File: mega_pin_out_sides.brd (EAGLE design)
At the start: 100 x 85 mm, 102 parts, among them T1 2N2222, T10 2N2222, T11 2N2222, T12 2N2222, T13 2N2222, T14 2N2222, T15 2N2222, T16 2N2222, T17 2N2222, T18 2N2222, T2 2N2222, T3 2N2222, T4 2N2222, T5 2N2222, T6 2N2222, T7 2N2222, T8 2N2222, T9 2N2222

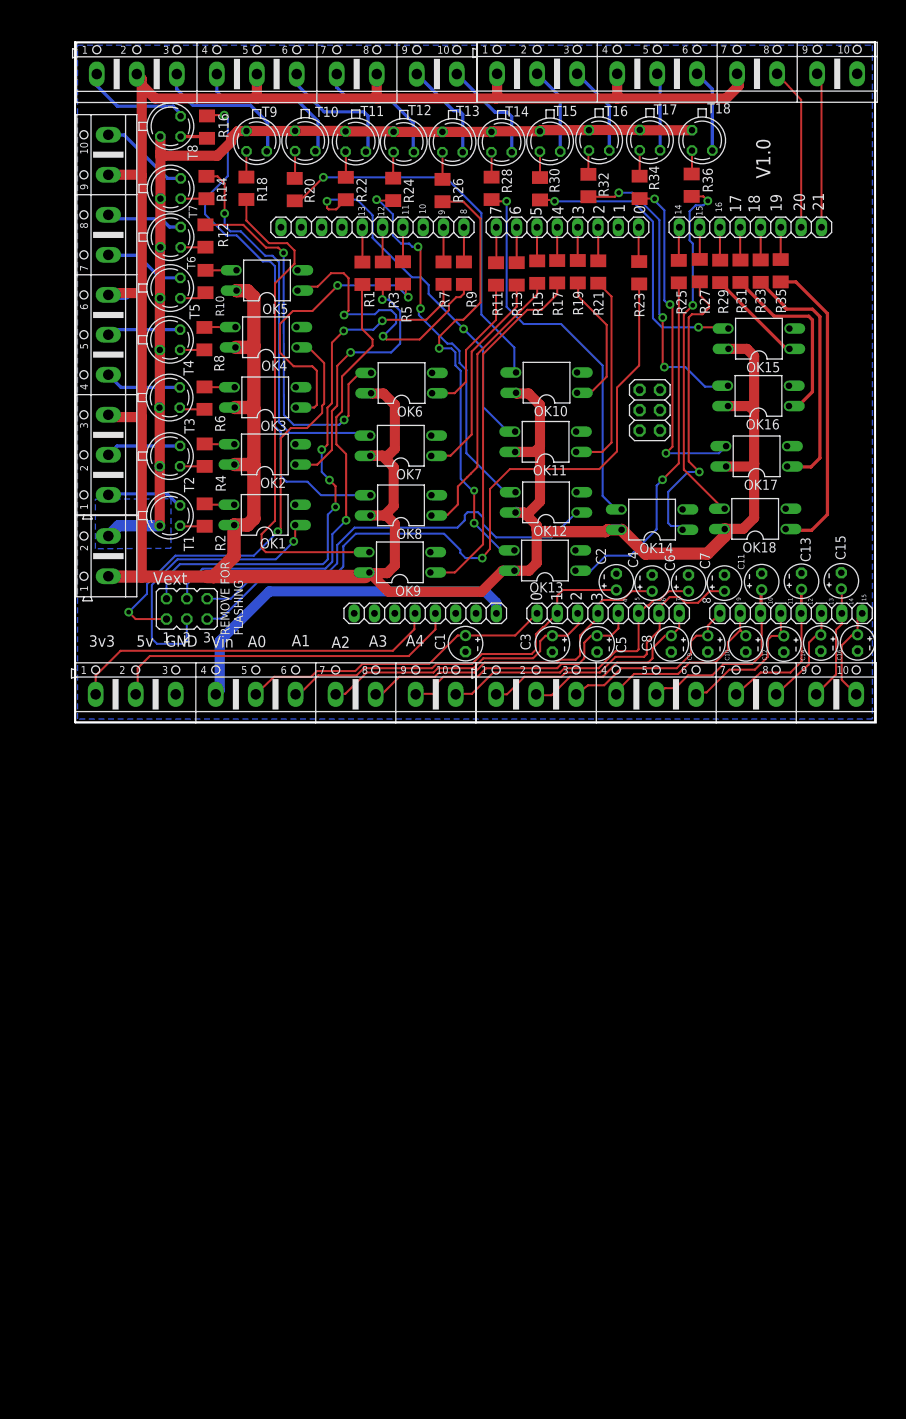
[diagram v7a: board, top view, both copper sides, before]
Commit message: [SIDES] Review of board and enhancements
- changed capacitors orientation. 
- Changed some pcb traces
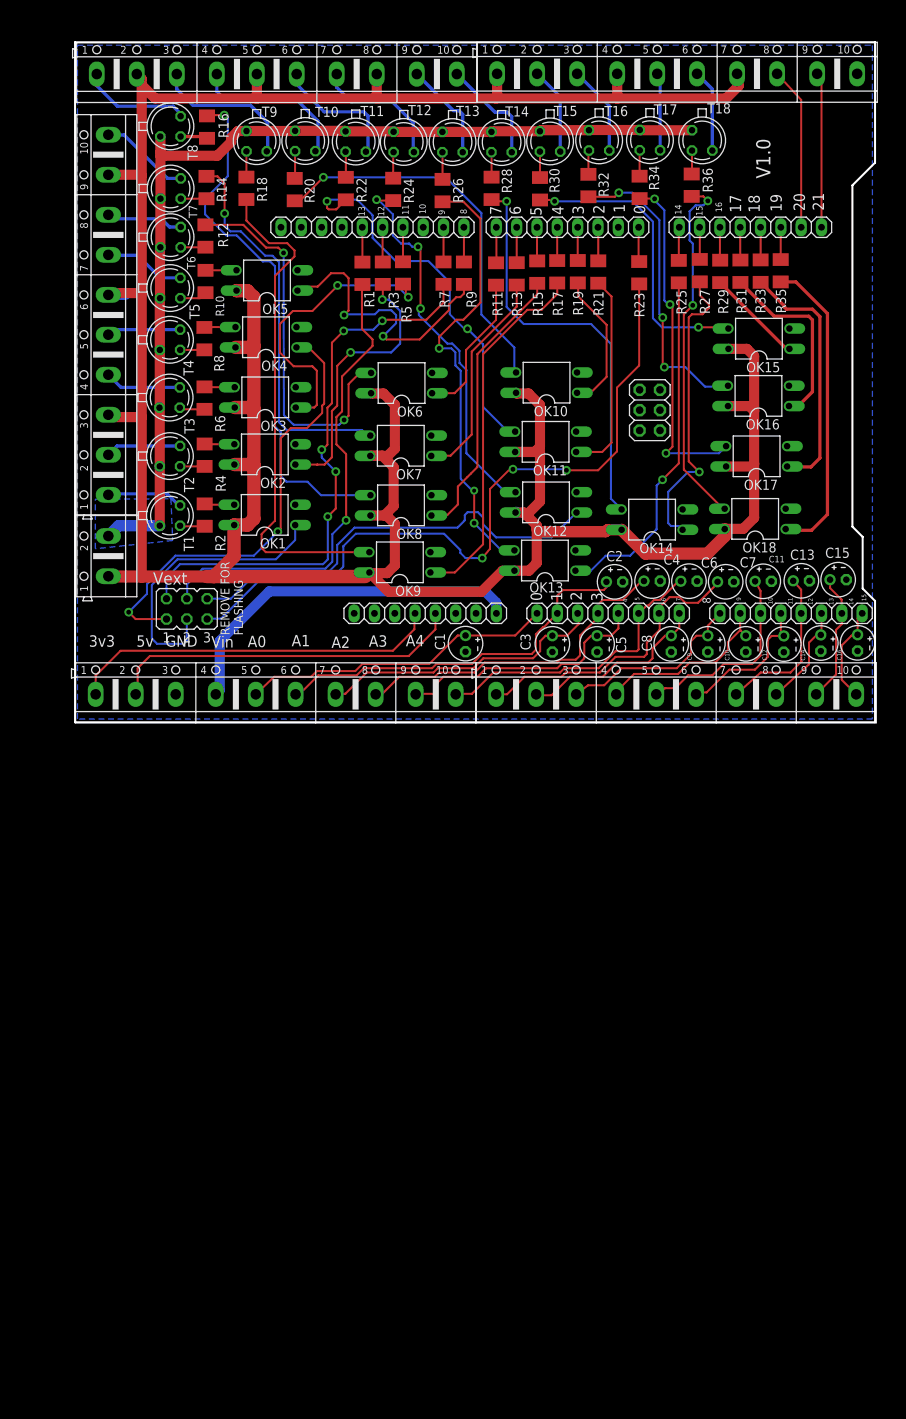
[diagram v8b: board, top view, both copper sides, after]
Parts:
- moved C15 0.42 mm to (95.4, 17.8), turned to 0 degrees
- moved C4 0.26 mm to (72.1, 17.7), turned to 0 degrees
- moved C6 0.24 mm to (76.7, 17.6), turned to 0 degrees
- moved C2 0.22 mm to (67.4, 17.6), turned to 0 degrees
- moved C7 0.22 mm to (81.3, 17.6), turned to 0 degrees
- moved C11 0.21 mm to (86.0, 17.6), turned to 0 degrees
- moved C13 0.06 mm to (90.8, 17.7), turned to 0 degrees
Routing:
- net N$39: track 46.0 -> 47.9 mm
- net A10: track 26.2 -> 24.4 mm
- net A14: track 14.5 -> 16.3 mm
- net A12: track 21.8 -> 20.3 mm
- net N$51: track 50.7 -> 52.2 mm
- net N$5: track 34.1 -> 34.6 mm
- net N$44: track 90.7 -> 90.8 mm, vias 1 -> 3
- net N$9: vias 1 -> 0
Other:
- outline, holes or cut-outs redrawn
